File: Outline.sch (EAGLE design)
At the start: 44 parts, among them CN1 0675031020, IC1 ATXMEGA32A4U-AU, IC2 ST1480ACDR, J1 RJHSE5080, Q1 BC817-16, U1 NCP1117DTAG @ 3.3v, U2 NCP1117DTAG @ 12v, X1 0470531000

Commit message: Version 2
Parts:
- C10, C12, C8: value 10uf 50v -> 10uF; device SparkFun:CAP_POLD -> SparkFun:CAP_POLC
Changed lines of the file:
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@@
 <grid distance="0.01" unitdist="inch" unit="inch" style="lines" multiple="1" display="no" altdistance="0.01" altunitdist="inch" altunit="inch"/>
 <layers>
-<layer number="1" name="Top" color="4" fill="1" visible="no" active="no"/>
-<layer number="16" name="Bottom" color="1" fill="1" visible="no" active="no"/>
-<layer number="17" name="Pads" color="2" fill="1" visible="no" active="no"/>
-<layer number="18" name="Vias" color="2" fill="1" visible="no" active="no"/>
-<layer number="19" name="Unrouted" color="6" fill="1" visible="no" active="no"/>
-<layer number="20" name="Dimension" color="15" fill="1" visible="no" active="no"/>
-<layer number="21" name="tPlace" color="14" fill="0" visible="no" active="no"/>
-<layer number="22" name="bPlace" color="7" fill="1" visible="no" active="no"/>
-<layer number="23" name="tOrigins" color="15" fill="1" visible="no" active="no"/>
-<layer number="24" name="bOrigins" color="15" fill="1" visible="no" active="no"/>
-<layer number="25" name="tNames" color="7" fill="1" visible="no" active="no"/>
-<layer number="26" name="bNames" color="7" fill="1" visible="no" active="no"/>
-<layer number="27" name="tValues" color="7" fill="1" visible="no" active="no"/>
-<layer number="28" name="bValues" color="7" fill="1" visible="no" active="no"/>
+<layer number="1" name="Top" color="4" fill="1" visible="yes" active="no"/>
+<layer number="16" name="Bottom" color="1" fill="1" visible="yes" active="no"/>
+<layer number="17" name="Pads" color="2" fill="1" visible="yes" active="no"/>
+<layer number="18" name="Vias" color="2" fill="1" visible="yes" active="no"/>
+<layer number="19" name="Unrouted" color="6" fill="1" visible="yes" active="no"/>
+<layer number="20" name="Dimension" color="15" fill="1" visible="yes" active="no"/>
+<layer number="21" name="tPlace" color="7" fill="1" visible="yes" active="no"/>
+<layer number="22" name="bPlace" color="7" fill="1" visible="yes" active="no"/>
+<layer number="23" name="tOrigins" color="15" fill="1" visible="yes" active="no"/>
+<layer number="24" name="bOrigins" color="15" fill="1" visible="yes" active="no"/>
+<layer number="25" name="tNames" color="7" fill="1" visible="yes" active="no"/>
+<layer number="26" name="bNames" color="7" fill="1" visible="yes" active="no"/>
+<layer number="27" name="tValues" color="7" fill="1" visible="yes" active="no"/>
+<layer number="28" name="bValues" color="7" fill="1" visible="yes" active="no"/>
 <layer number="29" name="tStop" color="7" fill="3" visible="no" active="no"/>
 <layer number="30" name="bStop" color="7" fill="6" visible="no" active="no"/>
@@
 <layer number="35" name="tGlue" color="7" fill="4" visible="no" active="no"/>
 <layer number="36" name="bGlue" color="7" fill="5" visible="no" active="no"/>
-<layer number="37" name="tTest" color="7" fill="1" visible="no" active="no"/>
-<layer number="38" name="bTest" color="7" fill="1" visible="no" active="no"/>
+<layer number="37" name="tTest" color="7" fill="1" visible="yes" active="no"/>
+<layer number="38" name="bTest" color="7" fill="1" visible="yes" active="no"/>
 <layer number="39" name="tKeepout" color="4" fill="11" visible="no" active="no"/>
 <layer number="40" name="bKeepout" color="1" fill="11" visible="no" active="no"/>
@@
 <layer number="44" name="Drills" color="7" fill="1" visible="no" active="no"/>
 <layer number="45" name="Holes" color="7" fill="1" visible="no" active="no"/>
-<layer number="46" name="Milling" color="3" fill="1" visible="no" active="no"/>
-<layer number="47" name="Measures" color="7" fill="1" visible="no" active="no"/>
-<layer number="48" name="Document" color="7" fill="1" visible="no" active="no"/>
-<layer number="49" name="Reference" color="7" fill="1" visible="no" active="no"/>
-<layer number="50" name="dxf" color="7" fill="1" visible="no" active="no"/>
-<layer number="51" name="tDocu" color="14" fill="0" visible="no" active="no"/>
-<layer number="52" name="bDocu" color="7" fill="1" visible="no" active="no"/>
-<layer number="53" name="tGND_GNDA" color="7" fill="9" visible="no" active="no"/>
-<layer number="54" name="bGND_GNDA" color="1" fill="9" visible="no" active="no"/>
-<layer number="56" name="wert" color="7" fill="1" visible="no" active="no"/>
+<layer number="46" name="Milling" color="3" fill="1" visible="yes" active="no"/>
+<layer number="47" name="Measures" color="7" fill="1" visible="yes" active="no"/>
+<layer number="48" name="Document" color="7" fill="1" visible="yes" active="no"/>
+<layer number="49" name="Reference" color="7" fill="1" visible="yes" active="no"/>
+<layer number="50" name="dxf" color="7" fill="1" visible="yes" active="no"/>
+<layer number="51" name="tDocu" color="7" fill="1" visible="yes" active="no"/>
+<layer number="52" name="bDocu" color="7" fill="1" visible="yes" active="no"/>
+<layer number="53" name="tGND_GNDA" color="7" fill="9" visible="yes" active="no"/>
+<layer number="54" name="bGND_GNDA" color="1" fill="9" visible="yes" active="no"/>
+<layer number="56" name="wert" color="7" fill="1" visible="yes" active="no"/>
 <layer number="91" name="Nets" color="2" fill="1" visible="yes" active="yes"/>
 <layer number="92" name="Busses" color="1" fill="1" visible="yes" active="yes"/>
@@
 <part name="GND12" library="supply1" deviceset="GND" device=""/>
 <part name="IND1" library="TechIsCool" deviceset="INDUCTOR" device="" value="68uH 760mA"/>
-<part name="C8" library="SparkFun" deviceset="CAP_POL" device="D" value="10uf 50v"/>
+<part name="C8" library="SparkFun" deviceset="CAP_POL" device="C" value="10uF"/>
 <part name="SC_D" library="TechIsCool" deviceset="SCHOTTYKY" device="" value="1PS74SB23"/>
 <part name="P+5" library="supply1" deviceset="+15V" device=""/>
@@
 <part name="GND15" library="supply1" deviceset="GND" device=""/>
 <part name="IND2" library="TechIsCool" deviceset="INDUCTOR" device="" value="68uH 760mA"/>
-<part name="C10" library="SparkFun" deviceset="CAP_POL" device="D" value="10uf 50v"/>
+<part name="C10" library="SparkFun" deviceset="CAP_POL" device="C" value="10uF"/>
 <part name="SC_D1" library="TechIsCool" deviceset="SCHOTTYKY" device="" value="1PS74SB23"/>
 <part name="P+4" library="supply1" deviceset="+15V" device=""/>
@@
 <part name="GND18" library="supply1" deviceset="GND" device=""/>
 <part name="IND3" library="TechIsCool" deviceset="INDUCTOR" device="" value="68uH 760mA"/>
-<part name="C12" library="SparkFun" deviceset="CAP_POL" device="D" value="10uf 50v"/>
+<part name="C12" library="SparkFun" deviceset="CAP_POL" device="C" value="10uF"/>
 <part name="SC_D2" library="TechIsCool" deviceset="SCHOTTYKY" device="" value="1PS74SB23"/>
 <part name="P+6" library="supply1" deviceset="+15V" device=""/>
@@
 <pinref part="C14" gate="G$1" pin="P$1"/>
 <pinref part="C14" gate="G$1" pin="P$1"/>
+<junction x="93.218" y="76.454"/>
 <pinref part="IC1" gate="G$1" pin="AVCC"/>
 <wire x1="90.678" y1="76.454" x2="93.218" y2="76.454" width="0.1524" layer="91"/>
-<pinref part="+3V3" gate="G$1" pin="+3V3"/>
-<wire x1="93.218" y1="81.788" x2="93.218" y2="76.454" width="0.1524" layer="91"/>
 <pinref part="C1" gate="G$1" pin="P$1"/>
 <pinref part="IC1" gate="G$1" pin="VCC@1"/>
@@
 <wire x1="93.218" y1="63.754" x2="90.678" y2="63.754" width="0.1524" layer="91"/>
 <wire x1="93.218" y1="66.294" x2="93.218" y2="63.754" width="0.1524" layer="91"/>
-<junction x="93.218" y="68.834"/>
-<junction x="93.218" y="66.294"/>
-<junction x="93.218" y="63.754"/>
-<junction x="93.218" y="76.454"/>
+<pinref part="+3V3" gate="G$1" pin="+3V3"/>
+<wire x1="93.218" y1="81.788" x2="93.218" y2="76.454" width="0.1524" layer="91"/>
 </segment>
 </net>

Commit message: Version 3
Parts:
- removed U$1: LABEL_JUMPER_1X3, dp_devices:LABEL_JUMPER_1X3
- removed X1: 0470531000, con-molex:KK-156-4
- added J2: J2, TechIsCool:470531000
- added PDI: AVR_PDI, TechIsCool:AVR_PDI
- added R13: 4.7k Ohm, nonolith:RESISTOR0603
- added R14: 11.8k, nonolith:RESISTOR0603
- added R15: 10k, nonolith:RESISTOR0603
- C1, C14, C6, C7: device nonolith:CAP_CERAMIC0805 -> SparkFun:CAP0603-CAP
- CN1: device adafruit:USBMINIB -> TechIsCool:USB_MINI_B
- J1: device con-amp:520426-4 -> TechIsCool:AMP_RJ45
- JP1: value (none) -> JUMPER_3; device jumper:JP2E -> TechIsCool:JUMPER_3
- R1, R8: value 300 mOhm -> 300m Ohm
- U$2: value AVR_PDI -> DS18B20; device TechIsCool:AVR_PDI -> TechIsCool:DS18B20
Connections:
- net N$16 renamed USB+
- net N$19 renamed USB-
- removed net N$17: IC2.B, J1.5
- removed net N$18: IC2.A, J1.6
- removed net N$23: IC1.RXD0/OC0C/PE2, IC2.RO
- removed net N$24: IC1.TXD0/OC0D/PE3, IC2.DE
- new net ONE_WIRE_TEMP: IC1.PC4/OC1A/#SS, R13.1, U$2.DQ
- new net RS485_N: IC2.B, J1.1
- new net RS485_P: IC2.A, J1.2
- new net RX: IC1.PC2/OC0C/RXD0, IC2.RO
- new net TX: IC1.PC3/OC0D/TXD0, IC2.DI
- new net VBUS_SENSE: IC1.XCK1/MOSI/PD5, R14.2, R15.1
- net +12V: now also J2G$3.S; no longer X1-3.S
- net +15V: now also J1.7, J1.8; no longer J1.1, J1.2
- net +3V3: now also C1.1, C14.1, C6.1, C7.1, PDI.VCC, R13.2, U$2.VDD; no longer C1.P$1, C14.P$1, C6.P$1, C7.P$1, U$2.VCC
- net +5V: now also R14.1
- net FAN_PWM: now also J2G$1.S; no longer X1-1.S
- net FAN_RPM: now also IC1.TXD0/OC0D/PE3; no longer IC1.PC4/OC1A/#SS
- net GND: now also C1.2, C14.2, C6.2, C7.2, J1.5, J1.6, J2G$4.S, PDI.GND, R15.2; no longer C1.P$2, C14.P$2, C6.P$2, C7.P$2, J1.7, J1.8, X1-4.S
- net N$20: now also PDI.PDI_D; no longer U$2.PDI_D
- net N$22: now also PDI.PDI_CLK; no longer U$2.PDI_CLK
- net N$25: now also J2G$2.S; no longer X1-2.S
- net RX_EN: now also IC1.PA5/ADC5; no longer IC1.OC0A/SDA/PE0
- net TX_EN: now also IC1.PA6/ADC6, IC2.DE; no longer IC1.XCK0/OC0B/SCL/PE1, IC2.DI
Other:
- moved on the sheet: CN1, J1

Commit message: Version 4
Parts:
- added C11, C13, C15, C9: .1uF, SparkFun:CAP0603-CAP
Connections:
- net +12V: now also C15.1
- net +15V: now also C13.1
- net +3V3: now also C9.1
- net GND: now also C11.2, C13.2, C15.2, C9.2
- net N$21: now also C11.1
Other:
- moved on the sheet: C2, C3, C4, C5, JP1, R3, R4, R5

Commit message: Version 4.1
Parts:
- removed Q1: BC817-16, dp_devices:TRANSISTOR_BJT_NPN-SOT-23-BEC
- removed R7: 1k Ohm, nonolith:RESISTOR0603
- added U$1: DMG1012T, TechIsCool:DMG1012T
- R2: value 102k Ohm -> 15 Ohms
- R3: value 62k Ohm -> 9.09 Ohms
- R4: value 102k Ohm -> 102 Ohms
- R5: value 11.8k Ohm -> 11.8 Ohms
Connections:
- new net N$4: R6.2, U$1.G
- net +12V: now also JP1.3
- net +15V: no longer JP1.3
- net FAN_SWITCH: now also R6.1; no longer R6.2
- net GND: now also U$1.S; no longer J2G$4.S, Q1.E, R7.2
- net N$2: no longer Q1.C
- net N$3: now also J2G$4.S, U$1.D; no longer Q1.B, R6.1, R7.1
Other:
- moved on the sheet: R10, R11, R4, R6

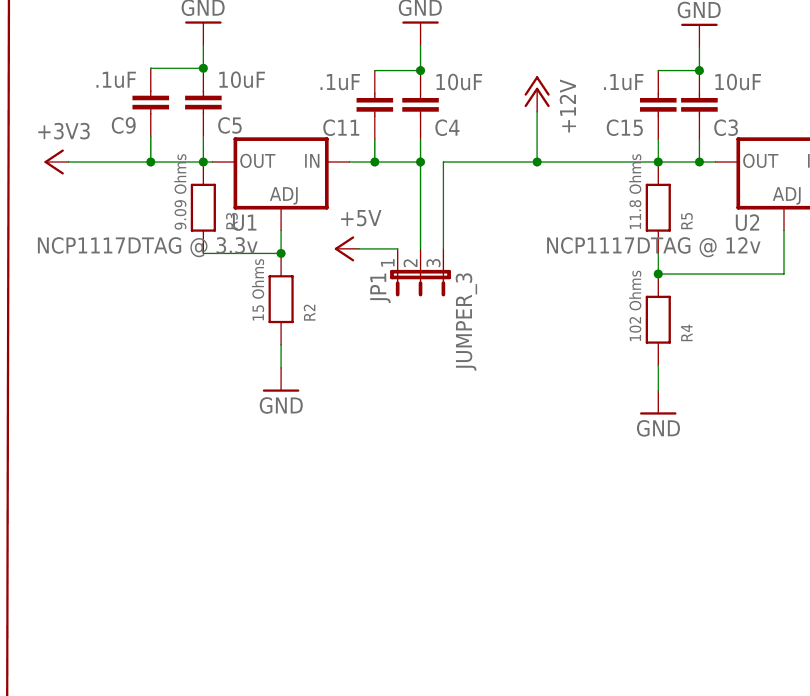
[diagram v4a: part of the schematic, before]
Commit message: Cleaned Up some
Still have a trace broken though
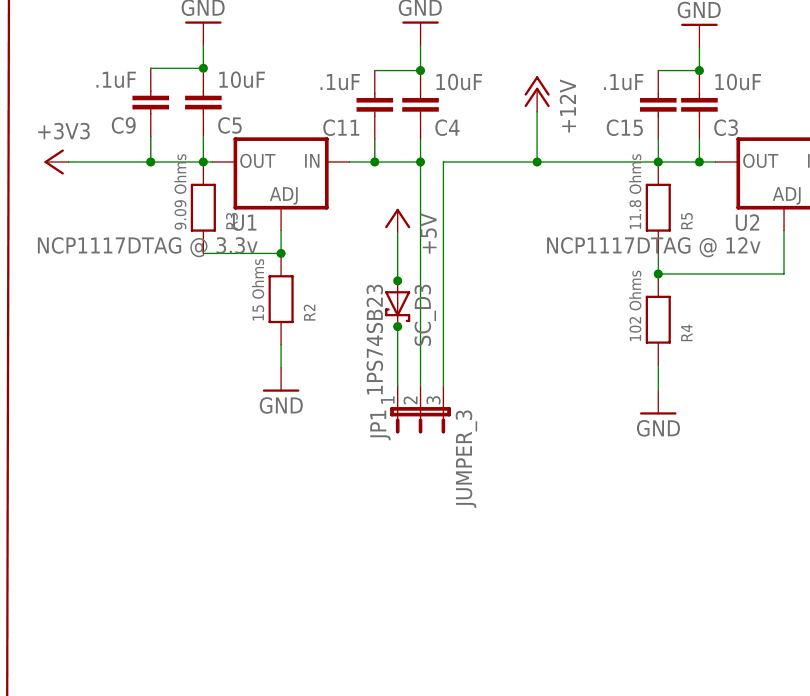
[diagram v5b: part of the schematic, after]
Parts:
- added SC_D3: 1PS74SB23, TechIsCool:SCHOTTKY_2
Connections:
- new net N$6: JP1.1, SC_D3.C
- net +5V: now also SC_D3.A; no longer JP1.1
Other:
- moved on the sheet: JP1
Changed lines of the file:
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@@
 <part name="U$1" library="TechIsCool" deviceset="DMG1012T" device=""/>
 <part name="R6" library="nonolith" deviceset="RESISTOR" device="0603" value="1k Ohm"/>
+<part name="SC_D3" library="TechIsCool" deviceset="SCHOTTKY_2" device="" value="1PS74SB23"/>
 </parts>
 <sheets>
@@
 <instance part="CN1" gate="G$1" x="116.078" y="119.38" rot="R270"/>
 <instance part="GND21" gate="1" x="110.998" y="106.68"/>
-<instance part="JP1" gate="G$1" x="193.04" y="66.04" rot="MR180"/>
-<instance part="P+8" gate="1" x="183.642" y="68.58" rot="MR270"/>
+<instance part="JP1" gate="G$1" x="193.04" y="50.8" rot="MR180"/>
+<instance part="P+8" gate="1" x="190.5" y="72.898" rot="MR0"/>
 <instance part="P+9" gate="1" x="121.158" y="90.424" rot="R180"/>
 <instance part="PDI" gate="G$1" x="14.986" y="86.868" rot="R90"/>
@@
 <instance part="U$1" gate="G$1" x="111.506" y="160.02"/>
 <instance part="R6" gate="G$1" x="101.092" y="157.48"/>
+<instance part="SC_D3" gate="G$1" x="190.5" y="62.484" rot="R270"/>
 </instances>
 <busses>
@@
 <wire x1="205.994" y1="83.82" x2="205.994" y2="78.232" width="0.1524" layer="91"/>
 <pinref part="JP1" gate="G$1" pin="3"/>
-<wire x1="195.58" y1="78.232" x2="195.58" y2="68.58" width="0.1524" layer="91"/>
+<wire x1="195.58" y1="78.232" x2="195.58" y2="53.34" width="0.1524" layer="91"/>
 <pinref part="U2" gate="G$1" pin="OUT"/>
 <wire x1="225.806" y1="78.232" x2="224.028" y2="78.232" width="0.1524" layer="91"/>
@@
 <wire x1="193.04" y1="80.772" x2="193.04" y2="78.232" width="0.1524" layer="91"/>
 <pinref part="JP1" gate="G$1" pin="2"/>
-<wire x1="193.04" y1="78.232" x2="193.04" y2="68.58" width="0.1524" layer="91"/>
+<wire x1="193.04" y1="78.232" x2="193.04" y2="53.34" width="0.1524" layer="91"/>
 <junction x="193.04" y="78.232"/>
 <pinref part="C11" gate="G$1" pin="1"/>
@@
 </net>
 <net name="+5V" class="0">
-<segment>
-<pinref part="JP1" gate="G$1" pin="1"/>
-<pinref part="P+8" gate="1" pin="+5V"/>
-<wire x1="190.5" y1="68.58" x2="186.182" y2="68.58" width="0.1524" layer="91"/>
-</segment>
 <segment>
 <pinref part="CN1" gate="G$1" pin="VBUS"/>
@@
 <wire x1="121.158" y1="96.52" x2="121.158" y2="92.964" width="0.1524" layer="91"/>
 <junction x="121.158" y="96.52"/>
+</segment>
+<segment>
+<pinref part="SC_D3" gate="G$1" pin="A"/>
+<pinref part="SC_D3" gate="G$1" pin="A"/>
+<pinref part="SC_D3" gate="G$1" pin="A"/>
+<pinref part="SC_D3" gate="G$1" pin="A"/>
+<pinref part="P+8" gate="1" pin="+5V"/>
+<wire x1="190.5" y1="70.358" x2="190.5" y2="65.024" width="0.1524" layer="91"/>
+<junction x="190.5" y="65.024"/>
 </segment>
 </net>
@@
 </segment>
 </net>
+<net name="N$6" class="0">
+<segment>
+<pinref part="SC_D3" gate="G$1" pin="C"/>
+<pinref part="SC_D3" gate="G$1" pin="C"/>
+<pinref part="JP1" gate="G$1" pin="1"/>
+<wire x1="190.5" y1="59.944" x2="190.5" y2="53.34" width="0.1524" layer="91"/>
+<junction x="190.5" y="59.944"/>
+</segment>
+</net>
